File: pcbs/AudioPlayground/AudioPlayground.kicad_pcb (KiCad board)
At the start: 6 copper layers, 69.7 x 22.9 mm, 141 parts, among them J1 Conn_01x07_Socket, J2 Conn_Battery, J3 USB_C_Receptacle_USB2.0_14P, J5 Conn_01x12_Pin, J7 Conn_01x16_Pin, J9 Conn_01x07_Socket, U1 nRF5340-QKxx, U10 MCP73831-2-OT, U11 SN74LVC1G126DRYR(UMW), U12 AP2280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

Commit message: Fix USB Pullups
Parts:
- R15, R16, R17: value 51k -> 10k
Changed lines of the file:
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@@
 			)
 		)
-		(property "Value" "51k"
+		(property "Value" "10k"
 			(at 0 1.17 0)
 			(layer "F.SilkS")
@@
 			)
 		)
-		(property "LCSC" "C25794"
+		(property "LCSC" "C25744"
 			(at 0 0 0)
 			(unlocked yes)
@@
 			)
 		)
-		(property "Value" "51k"
+		(property "Value" "10k"
 			(at 0 1.17 90)
 			(layer "F.SilkS")
@@
 			)
 		)
-		(property "LCSC" "C25794"
+		(property "LCSC" "C25744"
 			(at 0 0 90)
 			(unlocked yes)
@@
 			)
 		)
-		(property "Value" "51k"
+		(property "Value" "10k"
 			(at 0 1.17 90)
 			(layer "F.SilkS")
@@
 			)
 		)
-		(property "LCSC" "C25794"
+		(property "LCSC" "C25744"
 			(at 0 0 270)
 			(unlocked yes)

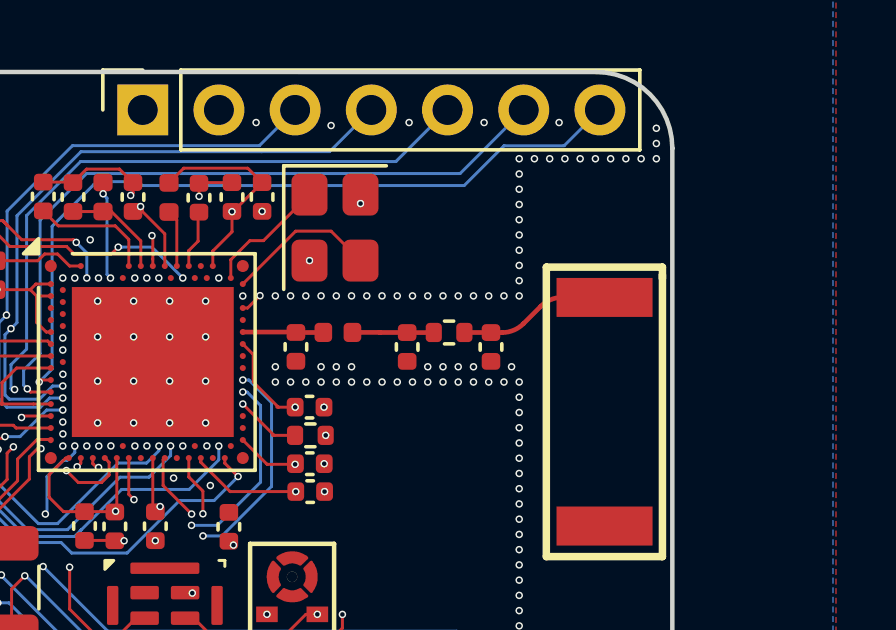
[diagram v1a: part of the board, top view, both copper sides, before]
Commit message: Fix Antenna Trace
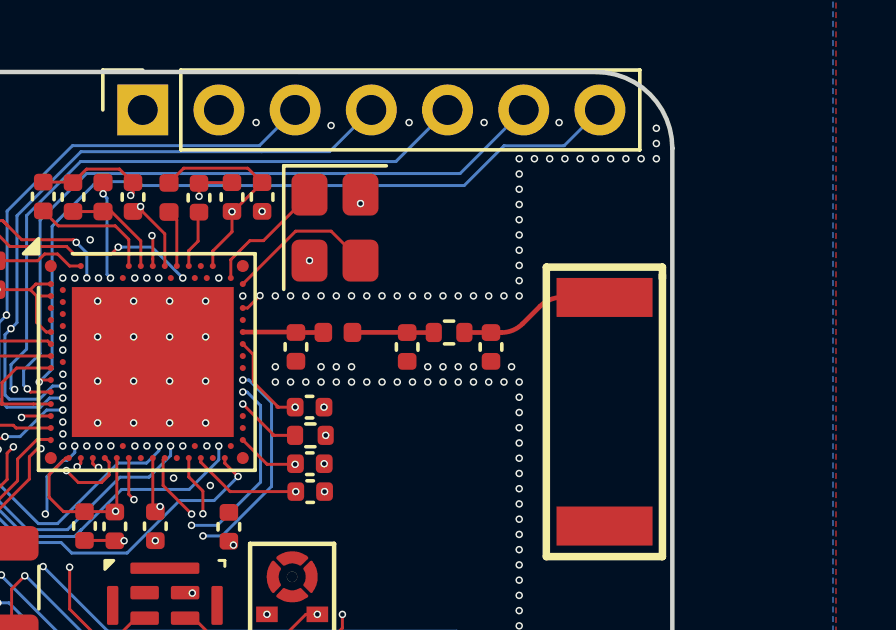
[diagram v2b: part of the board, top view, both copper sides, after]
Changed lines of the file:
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@@
 	)
 	(segment
-		(start 150.376171 130.151727)
-		(end 152.131327 130.151727)
-		(width 0.1565)
+		(start 152.131327 130.151727)
+		(end 152.146749 130.167149)
+		(width 0.1204)
 		(layer "F.Cu")
 		(net 11)
 	)
 	(segment
-		(start 152.131327 130.151727)
-		(end 152.146749 130.167149)
+		(start 153.058549 130.167149)
+		(end 153.061149 130.164549)
+		(width 0.1204)
+		(layer "F.Cu")
+		(net 11)
+	)
+	(segment
+		(start 152.146749 130.167149)
+		(end 153.058549 130.167149)
 		(width 0.1565)
 		(layer "F.Cu")
@@
 	)
 	(segment
-		(start 153.058549 130.167149)
-		(end 153.061149 130.164549)
-		(width 0.1565)
-		(layer "F.Cu")
-		(net 11)
-	)
-	(segment
-		(start 152.146749 130.167149)
-		(end 153.058549 130.167149)
+		(start 150.376171 130.151727)
+		(end 152.131327 130.151727)
 		(width 0.1565)
 		(layer "F.Cu")
@@
 	)
 	(segment
-		(start 154.938149 130.164549)
-		(end 154.940749 130.161949)
+		(start 155.855149 130.169749)
+		(end 156.739549 130.169749)
 		(width 0.1565)
 		(layer "F.Cu")
@@
 	(segment
 		(start 154.031149 130.164549)
-		(end 154.938149 130.164549)
+		(end 155.849949 130.164549)
 		(width 0.1565)
 		(layer "F.Cu")
@@
 	)
 	(segment
-		(start 156.739549 130.169749)
-		(end 156.742149 130.167149)
-		(width 0.1565)
-		(layer "F.Cu")
-		(net 153)
-	)
-	(segment
-		(start 154.940749 130.167149)
-		(end 155.852549 130.167149)
-		(width 0.1565)
-		(layer "F.Cu")
-		(net 153)
-	)
-	(segment
-		(start 154.938149 130.164549)
-		(end 154.940749 130.167149)
-		(width 0.1565)
+		(start 155.849949 130.164549)
+		(end 155.855149 130.169749)
+		(width 0.1204)
 		(layer "F.Cu")
 		(net 153)
 	)
 	(segment
-		(start 155.855149 130.169749)
-		(end 156.739549 130.169749)
-		(width 0.1565)
+		(start 156.739549 130.169749)
+		(end 156.742149 130.167149)
+		(width 0.1204)
 		(layer "F.Cu")
 		(net 153)
@@
 	)
 	(segment
-		(start 161.019163 128.998749)
+		(start 160.993763 128.998749)
 		(end 162.433749 128.998749)
 		(width 0.1565)
@@
 	)
 	(segment
-		(start 159.726842 129.876856)
-		(end 160.312056 129.291642)
+		(start 159.701442 129.876856)
+		(end 160.286656 129.291642)
 		(width 0.1565)
 		(layer "F.Cu")
@@
 	(segment
 		(start 158.649149 130.169749)
-		(end 159.019735 130.169749)
+		(end 158.994335 130.169749)
 		(width 0.1565)
 		(layer "F.Cu")
@@
 		(start 158.646549 130.167149)
 		(end 158.649149 130.169749)
-		(width 0.1565)
+		(width 0.1204)
 		(layer "F.Cu")
 		(net 186)
 	)
 	(arc
-		(start 159.019735 130.169749)
-		(mid 159.402418 130.093629)
-		(end 159.726842 129.876856)
+		(start 160.286656 129.291642)
+		(mid 160.611079 129.074869)
+		(end 160.993763 128.998749)
 		(width 0.1565)
 		(layer "F.Cu")
@@
 	)
 	(arc
-		(start 161.019163 128.998749)
-		(mid 160.63648 129.074869)
-		(end 160.312056 129.291642)
+		(start 158.994335 130.169749)
+		(mid 159.377018 130.093629)
+		(end 159.701442 129.876856)
 		(width 0.1565)
 		(layer "F.Cu")
@@
 		(net 0)
 		(net_name "")
-		(layer "F.Cu")
+		(layers "F.Cu" "B.Cu" "In1.Cu" "In2.Cu" "In3.Cu" "In4.Cu")
 		(hatch edge 0.5)
 		(connect_pads thru_hole_only
@@
 			)
 		)
-	)
-	(zone
-		(net 0)
-		(net_name "")
-		(layers "B.Cu" "In1.Cu" "In2.Cu" "In3.Cu" "In4.Cu")
-		(hatch edge 0.5)
-		(connect_pads
-			(clearance 0)
-		)
-		(min_thickness 0.25)
-		(filled_areas_thickness no)
-		(keepout
-			(tracks allowed)
-			(vias allowed)
-			(pads allowed)
-			(copperpour not_allowed)
-			(footprints allowed)
-		)
-		(placement
-			(enabled no)
-			(sheetname "")
-		)
-		(fill
-			(thermal_gap 0.5)
-			(thermal_bridge_width 0.5)
-		)
-		(polygon
-			(pts
-				(xy 159.436549 129.328949) (xy 150.190949 129.328949) (xy 150.063949 129.455949) (xy 150.063949 130.852949)
-				(xy 150.190949 130.980121) (xy 159.436549 131.001095) (xy 159.792149 131.386349) (xy 159.792149 141.266949)
-				(xy 164.821349 141.266949) (xy 164.821349 124.604549) (xy 159.792149 124.604549) (xy 159.792149 128.973349)
-			)
-		)

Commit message: Add Test Points
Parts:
- added TP1: SDA, TestPoint:TestPoint_Pad_D1.0mm, F.Cu at (133.5, 129.1)
- added TP2: SCL, TestPoint:TestPoint_Pad_D1.0mm, F.Cu at (132.4, 130.8)
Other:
- board text added: "SCL"
- board text added: "SDA"

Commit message: Change Analog Switches
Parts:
- removed U18: SN74LVC1G126DRYR(UMW), SN74LVC1G126DRYR:SN74LVC1G126DRYR
- added J4: TC2030, Connector:Tag-Connect_TC2030-IDC-NL_2x03_P1.27mm_Vertical, F.Cu at (156.4, 136.0)
- added U21: SN74LVC1G66DRYR, C507245:SN74LVC1G66DRYR, F.Cu at (116.5, 138.3)
- U11, U13, U16, U17: value SN74LVC1G126DRYR(UMW) -> SN74LVC1G66DRYR; footprint SN74LVC1G126DRYR:SN74LVC1G126DRYR -> C507245:SN74LVC1G66DRYR
- moved U16 3.95 mm to (118.6, 136.4)
- moved U13 2.16 mm to (117.6, 140.3)
- moved U17 1.90 mm to (118.6, 138.3)
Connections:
- U11 pad 1: +3.3V_SWITCHED -> /Interface MCU/VCOM.RXD
- U11 pad 2: /Interface MCU/VCOM.TXD -> /MCU/VCOM.TXD
- U11 pad 4: /MCU/VCOM.RXD -> +3.3V_SWITCHED
- U13 pad 1: +3.3V_SWITCHED -> /Interface MCU/SWD.SWDIO
- U13 pad 2: /Interface MCU/VCOM.RXD -> /MCU/SWD.SWDIO
- U13 pad 4: /MCU/VCOM.TXD -> +3.3V_SWITCHED
- U16 pad 1: +3.3V_SWITCHED -> /Interface MCU/SWD.SWDCLK
- U16 pad 2: /Interface MCU/SWD.SWDIO -> /MCU/SWD.SWDCLK
- U16 pad 4: /MCU/SWD.SWDIO -> +3.3V_SWITCHED
- U17 pad 1: +3.3V_SWITCHED -> /Interface MCU/SWD.RESET
- U17 pad 2: /Interface MCU/SWD.SWDCLK -> /MCU/SWD.RESET
- U17 pad 4: /MCU/SWD.SWDCLK -> +3.3V_SWITCHED
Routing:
- net Net-(U2-RES): track 1.65 -> 43.6 mm, vias 0 -> 2
- net +3.3V_SWITCHED: track 100.1 -> 141.3 mm, vias 22 -> 21
- net Net-(U2-P109/TDO/SWO): track 0.00 -> 39.4 mm, vias 1 -> 2
- net Net-(U2-P300/TCK/SWCLK): track 0.00 -> 39.3 mm, vias 0 -> 2
- net Net-(U2-P108/TMS/SWDIO): track 7.15 -> 43.3 mm, vias 2 -> 3
- net /MCU/VCOM.TXD: track 38.2 -> 41.3 mm
- net +3.3V: track 80.1 -> 82.6 mm
- net /Interface MCU/VCOM.TXD: track 13.4 -> 15.1 mm
- net /Interface MCU/VCOM.RXD: track 15.3 -> 13.8 mm, vias 2 -> 3
- net /MCU/VCOM.RXD: track 35.3 -> 36.7 mm, vias 3 -> 4
- net /MCU/SWD.SWDIO: track 39.9 -> 40.8 mm, vias 3 -> 4
- net /MCU/SWD.SWDCLK: track 43.2 -> 44.0 mm
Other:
- board text added: "LE Audio Playground v2.1"
- board text removed: "LE Audio Playground v2.0"
